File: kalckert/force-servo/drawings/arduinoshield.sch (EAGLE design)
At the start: 27 parts, among them IC1 MCP604P, IC3 7806T

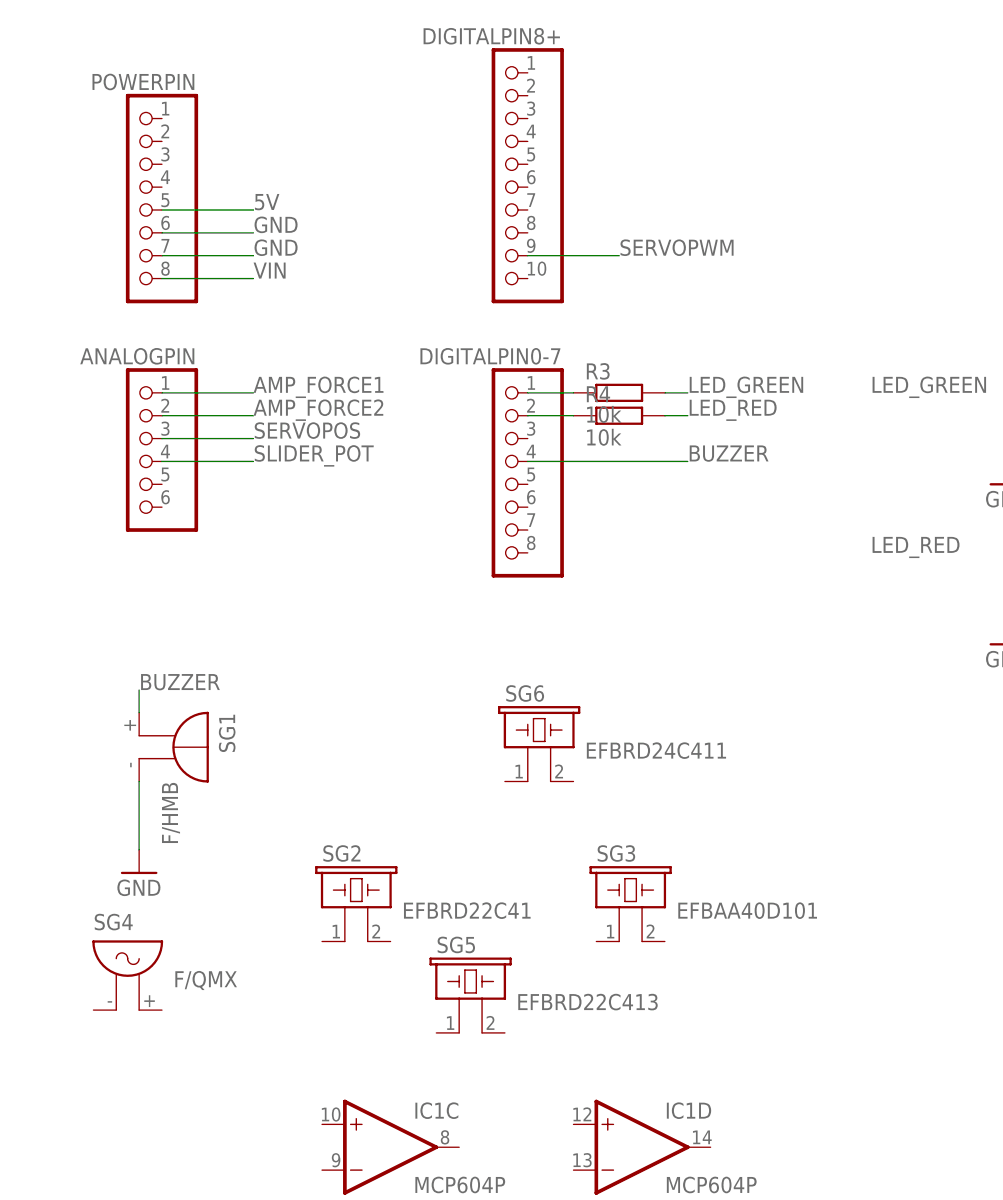
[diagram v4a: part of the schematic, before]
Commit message: Added hardware licensing files. Updated shematic to prevent autoreset of Arduino.
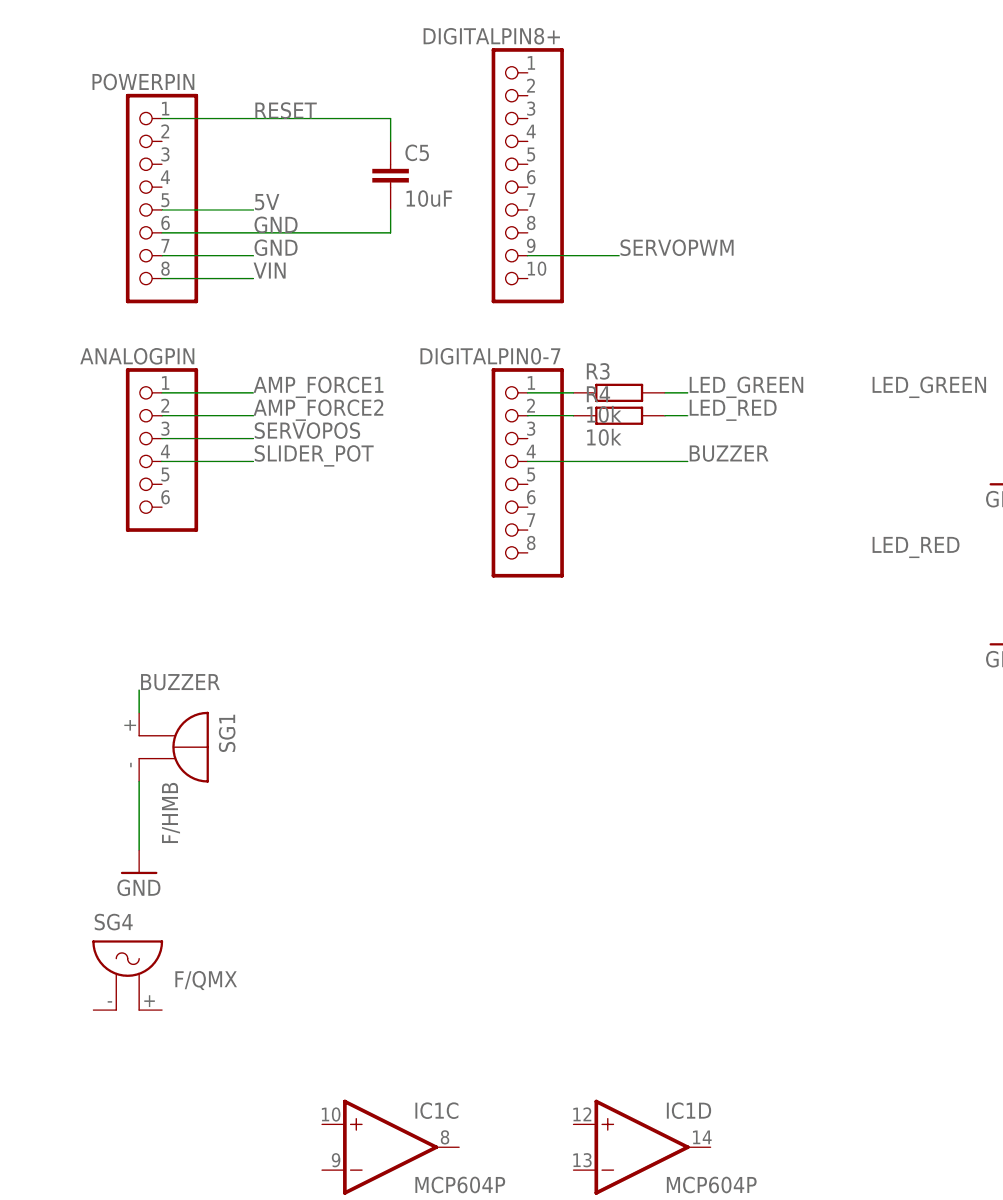
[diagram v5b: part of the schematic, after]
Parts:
- removed SG2: EFBRD22C41, buzzer:EFBRD22C41
- removed SG3: EFBAA40D101, buzzer:EFBAA40D101
- removed SG5: EFBRD22C413, buzzer:EFBRD22C413
- removed SG6: EFBRD24C411, buzzer:EFBRD24C411
- added C5: 10uF, resistor:C-EU025-025X050
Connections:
- new net RESET: C5.1, POWERPIN.1
- net GND: now also C5.2
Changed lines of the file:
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@@
 <part name="IC4" library="linear" deviceset="79*" device="T" technology="05"/>
 <part name="SG4" library="buzzer" deviceset="F/QMX" device=""/>
-<part name="SG2" library="buzzer" deviceset="EFB?" device="RD22C41"/>
-<part name="SG3" library="buzzer" deviceset="EFB?" device="AA40D101"/>
-<part name="SG5" library="buzzer" deviceset="EFB?" device="RD22C413"/>
-<part name="SG6" library="buzzer" deviceset="EFB?" device="RD24C411"/>
+<part name="C5" library="resistor" deviceset="C-EU" device="025-025X050" value="10uF"/>
 </parts>
 <sheets>
@@
 <instance part="IC4" gate="A1" x="53.34" y="33.02"/>
 <instance part="SG4" gate="G$1" x="139.7" y="53.34"/>
-<instance part="SG2" gate="G$1" x="165.1" y="60.96"/>
-<instance part="SG3" gate="G$1" x="195.58" y="60.96"/>
-<instance part="SG5" gate="G$1" x="177.8" y="50.8"/>
-<instance part="SG6" gate="G$1" x="185.42" y="78.74"/>
+<instance part="C5" gate="G$1" x="170.18" y="144.78"/>
 </instances>
 <busses>
@@
 <segment>
 <pinref part="POWERPIN" gate="A" pin="6"/>
-<wire x1="144.78" y1="137.16" x2="154.94" y2="137.16" width="0.1524" layer="91"/>
 <label x="154.94" y="137.16" size="1.778" layer="95"/>
+<pinref part="C5" gate="G$1" pin="2"/>
+<wire x1="144.78" y1="137.16" x2="170.18" y2="137.16" width="0.1524" layer="91"/>
+<wire x1="170.18" y1="137.16" x2="170.18" y2="139.7" width="0.1524" layer="91"/>
 </segment>
 <segment>
@@
 </segment>
 </net>
+<net name="RESET" class="0">
+<segment>
+<pinref part="POWERPIN" gate="A" pin="1"/>
+<pinref part="C5" gate="G$1" pin="1"/>
+<wire x1="144.78" y1="149.86" x2="170.18" y2="149.86" width="0.1524" layer="91"/>
+<wire x1="170.18" y1="149.86" x2="170.18" y2="147.32" width="0.1524" layer="91"/>
+<label x="154.94" y="149.86" size="1.778" layer="95"/>
+</segment>
+</net>

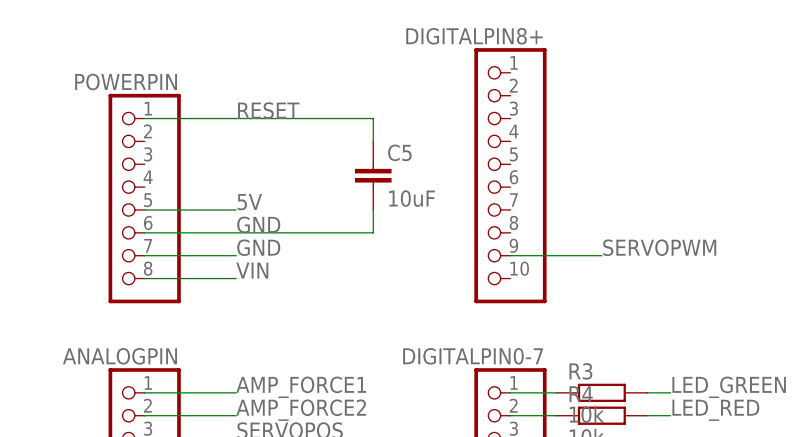
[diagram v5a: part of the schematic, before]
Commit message: Added a calibration sequence in the arduino program.
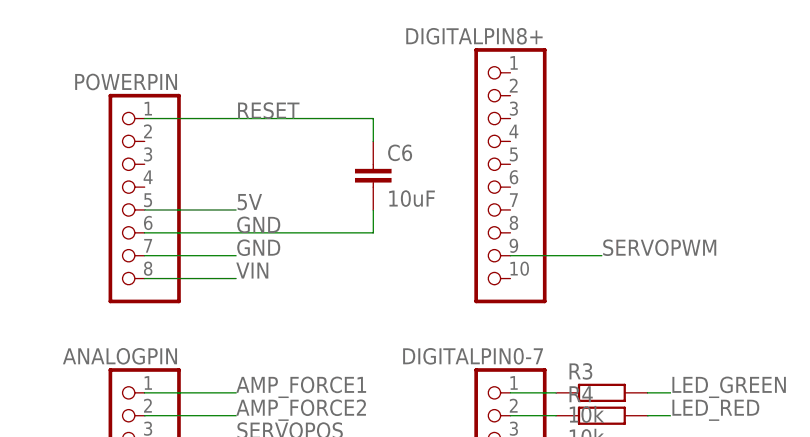
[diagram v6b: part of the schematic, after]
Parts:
- removed C5: 10uF, resistor:C-EU025-025X050
- added C6: 10uF, resistor:C-EU050-025X075
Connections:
- net GND: now also C6.2; no longer C5.2
- net RESET: now also C6.1; no longer C5.1
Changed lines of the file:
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@@
 <part name="IC4" library="linear" deviceset="79*" device="T" technology="05"/>
 <part name="SG4" library="buzzer" deviceset="F/QMX" device=""/>
-<part name="C5" library="resistor" deviceset="C-EU" device="025-025X050" value="10uF"/>
+<part name="C6" library="resistor" deviceset="C-EU" device="050-025X075" value="10uF"/>
 </parts>
 <sheets>
@@
 <instance part="IC4" gate="A1" x="53.34" y="33.02"/>
 <instance part="SG4" gate="G$1" x="139.7" y="53.34"/>
-<instance part="C5" gate="G$1" x="170.18" y="144.78"/>
+<instance part="C6" gate="G$1" x="170.18" y="144.78"/>
 </instances>
 <busses>
@@
 <pinref part="POWERPIN" gate="A" pin="6"/>
 <label x="154.94" y="137.16" size="1.778" layer="95"/>
-<pinref part="C5" gate="G$1" pin="2"/>
 <wire x1="144.78" y1="137.16" x2="170.18" y2="137.16" width="0.1524" layer="91"/>
 <wire x1="170.18" y1="137.16" x2="170.18" y2="139.7" width="0.1524" layer="91"/>
+<pinref part="C6" gate="G$1" pin="2"/>
 </segment>
 <segment>
@@
 <segment>
 <pinref part="POWERPIN" gate="A" pin="1"/>
-<pinref part="C5" gate="G$1" pin="1"/>
 <wire x1="144.78" y1="149.86" x2="170.18" y2="149.86" width="0.1524" layer="91"/>
 <wire x1="170.18" y1="149.86" x2="170.18" y2="147.32" width="0.1524" layer="91"/>
 <label x="154.94" y="149.86" size="1.778" layer="95"/>
-</segment>
-</net>
+<pinref part="C6" gate="G$1" pin="1"/>
+</segment>
+</net>

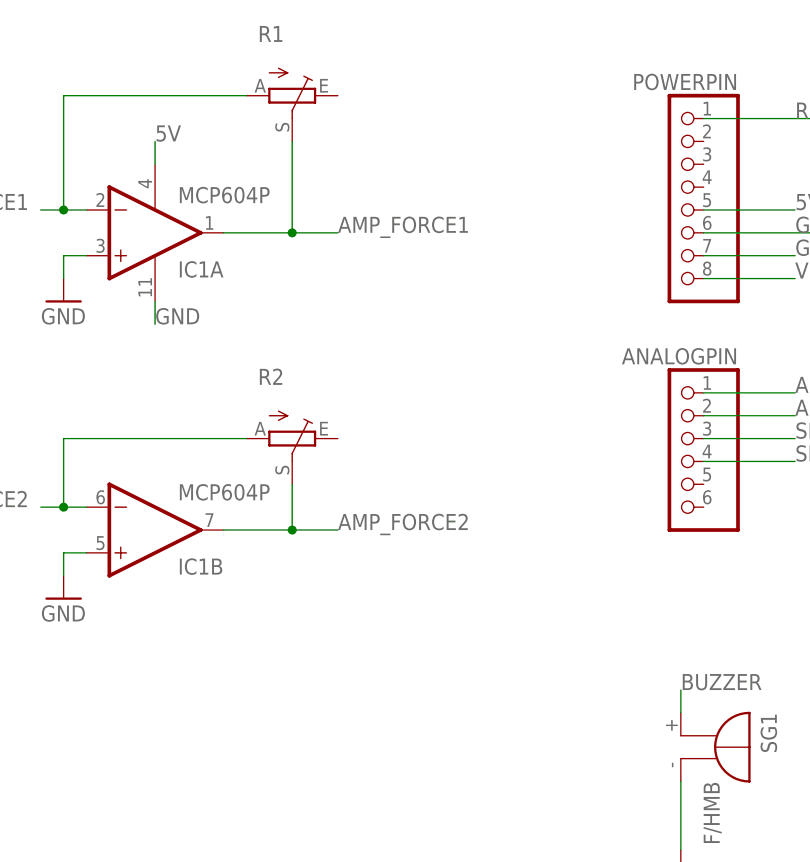
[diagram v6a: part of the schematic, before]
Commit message: Tuning the PD controller gains, not yet stable. Updated schematic with the LP filter.
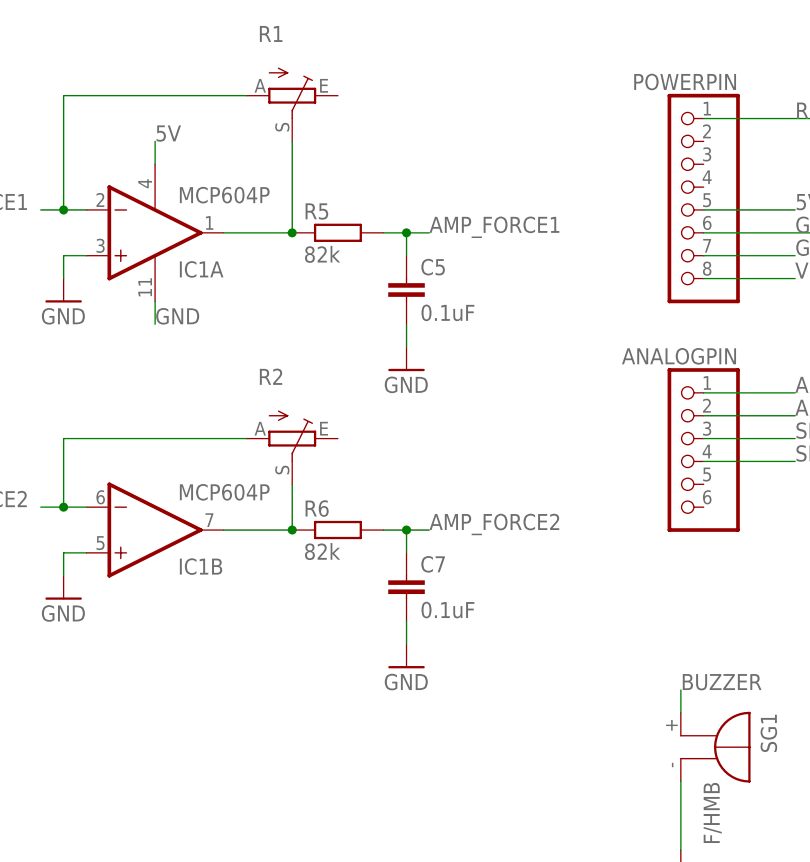
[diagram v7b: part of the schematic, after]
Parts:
- added C5, C7: 0.1uF, resistor:C-EU025-025X050
- added R5, R6: 82k, resistor:R-EU_0207/7
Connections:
- new net N$12: IC1A.OUT, R1.S, R5.1
- new net N$13: IC1B.OUT, R2.S, R6.1
- net AMP_FORCE1: now also C5.1, R5.2; no longer IC1A.OUT, R1.S
- net AMP_FORCE2: now also C7.1, R6.2; no longer IC1B.OUT, R2.S
- net GND: now also C5.2, C7.2
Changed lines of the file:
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@@
 <part name="SG4" library="buzzer" deviceset="F/QMX" device=""/>
 <part name="C6" library="resistor" deviceset="C-EU" device="050-025X075" value="10uF"/>
+<part name="R5" library="resistor" deviceset="R-EU_" device="0207/7" value="82k"/>
+<part name="R6" library="resistor" deviceset="R-EU_" device="0207/7" value="82k"/>
+<part name="C5" library="resistor" deviceset="C-EU" device="025-025X050" value="0.1uF"/>
+<part name="C7" library="resistor" deviceset="C-EU" device="025-025X050" value="0.1uF"/>
+<part name="GND8" library="supply1" deviceset="GND" device=""/>
+<part name="GND9" library="supply1" deviceset="GND" device=""/>
 </parts>
 <sheets>
@@
 <instance part="SG4" gate="G$1" x="139.7" y="53.34"/>
 <instance part="C6" gate="G$1" x="170.18" y="144.78"/>
+<instance part="R5" gate="G$1" x="104.14" y="137.16"/>
+<instance part="R6" gate="G$1" x="104.14" y="104.14"/>
+<instance part="C5" gate="G$1" x="111.76" y="132.08"/>
+<instance part="C7" gate="G$1" x="111.76" y="99.06"/>
+<instance part="GND8" gate="1" x="111.76" y="121.92"/>
+<instance part="GND9" gate="1" x="111.76" y="88.9"/>
 </instances>
 <busses>
@@
 <pinref part="GND7" gate="1" pin="GND"/>
 </segment>
+<segment>
+<pinref part="GND9" gate="1" pin="GND"/>
+<pinref part="C7" gate="G$1" pin="2"/>
+<wire x1="111.76" y1="91.44" x2="111.76" y2="93.98" width="0.1524" layer="91"/>
+</segment>
+<segment>
+<pinref part="GND8" gate="1" pin="GND"/>
+<pinref part="C5" gate="G$1" pin="2"/>
+<wire x1="111.76" y1="124.46" x2="111.76" y2="127" width="0.1524" layer="91"/>
+</segment>
 </net>
 <net name="VCCSERVO" class="0">
@@
 <net name="AMP_FORCE1" class="0">
 <segment>
-<pinref part="IC1" gate="A" pin="OUT"/>
-<wire x1="91.44" y1="137.16" x2="99.06" y2="137.16" width="0.1524" layer="91"/>
-<wire x1="99.06" y1="137.16" x2="99.06" y2="147.32" width="0.1524" layer="91"/>
-<pinref part="R1" gate="1" pin="S"/>
-<wire x1="99.06" y1="137.16" x2="104.14" y2="137.16" width="0.1524" layer="91"/>
-<junction x="99.06" y="137.16"/>
-<label x="104.14" y="137.16" size="1.778" layer="95"/>
-</segment>
-<segment>
 <pinref part="ANALOGPIN" gate="A" pin="1"/>
 <wire x1="144.78" y1="119.38" x2="154.94" y2="119.38" width="0.1524" layer="91"/>
 <label x="154.94" y="119.38" size="1.778" layer="95"/>
 </segment>
+<segment>
+<pinref part="R5" gate="G$1" pin="2"/>
+<wire x1="109.22" y1="137.16" x2="111.76" y2="137.16" width="0.1524" layer="91"/>
+<label x="114.3" y="137.16" size="1.778" layer="95"/>
+<pinref part="C5" gate="G$1" pin="1"/>
+<wire x1="111.76" y1="137.16" x2="114.3" y2="137.16" width="0.1524" layer="91"/>
+<wire x1="111.76" y1="134.62" x2="111.76" y2="137.16" width="0.1524" layer="91"/>
+<junction x="111.76" y="137.16"/>
+</segment>
 </net>
 <net name="AMP_FORCE2" class="0">
-<segment>
-<pinref part="R2" gate="1" pin="S"/>
-<wire x1="104.14" y1="104.14" x2="99.06" y2="104.14" width="0.1524" layer="91"/>
-<wire x1="99.06" y1="104.14" x2="99.06" y2="109.22" width="0.1524" layer="91"/>
-<pinref part="IC1" gate="B" pin="OUT"/>
-<wire x1="91.44" y1="104.14" x2="99.06" y2="104.14" width="0.1524" layer="91"/>
-<junction x="99.06" y="104.14"/>
-<label x="104.14" y="104.14" size="1.778" layer="95"/>
-</segment>
 <segment>
 <pinref part="ANALOGPIN" gate="A" pin="2"/>
 <wire x1="144.78" y1="116.84" x2="154.94" y2="116.84" width="0.1524" layer="91"/>
 <label x="154.94" y="116.84" size="1.778" layer="95"/>
+</segment>
+<segment>
+<pinref part="R6" gate="G$1" pin="2"/>
+<wire x1="109.22" y1="104.14" x2="111.76" y2="104.14" width="0.1524" layer="91"/>
+<label x="114.3" y="104.14" size="1.778" layer="95"/>
+<pinref part="C7" gate="G$1" pin="1"/>
+<wire x1="111.76" y1="104.14" x2="114.3" y2="104.14" width="0.1524" layer="91"/>
+<wire x1="111.76" y1="101.6" x2="111.76" y2="104.14" width="0.1524" layer="91"/>
+<junction x="111.76" y="104.14"/>
 </segment>
 </net>
@@
 </segment>
 </net>
+<net name="N$12" class="0">
+<segment>
+<pinref part="IC1" gate="A" pin="OUT"/>
+<pinref part="R5" gate="G$1" pin="1"/>
+<wire x1="91.44" y1="137.16" x2="99.06" y2="137.16" width="0.1524" layer="91"/>
+<pinref part="R1" gate="1" pin="S"/>
+<wire x1="99.06" y1="147.32" x2="99.06" y2="137.16" width="0.1524" layer="91"/>
+<junction x="99.06" y="137.16"/>
+</segment>
+</net>
+<net name="N$13" class="0">
+<segment>
+<pinref part="R2" gate="1" pin="S"/>
+<pinref part="R6" gate="G$1" pin="1"/>
+<wire x1="99.06" y1="109.22" x2="99.06" y2="104.14" width="0.1524" layer="91"/>
+<pinref part="IC1" gate="B" pin="OUT"/>
+<wire x1="99.06" y1="104.14" x2="91.44" y2="104.14" width="0.1524" layer="91"/>
+<junction x="99.06" y="104.14"/>
+</segment>
+</net>
